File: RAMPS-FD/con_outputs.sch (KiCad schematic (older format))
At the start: 28 parts, among them P218 EXT3, P403 D9_EXT, P404 D8_HB, P405 D10_EXT1, Q201 IRLB8743PBF, Q202 IRLB8743PBF, Q203 IRLB8743PBF, Q204 2N7002, Q205 2N7002, Q206 IRLB8743PBF, Q501 2N7002, Q502 2N7002

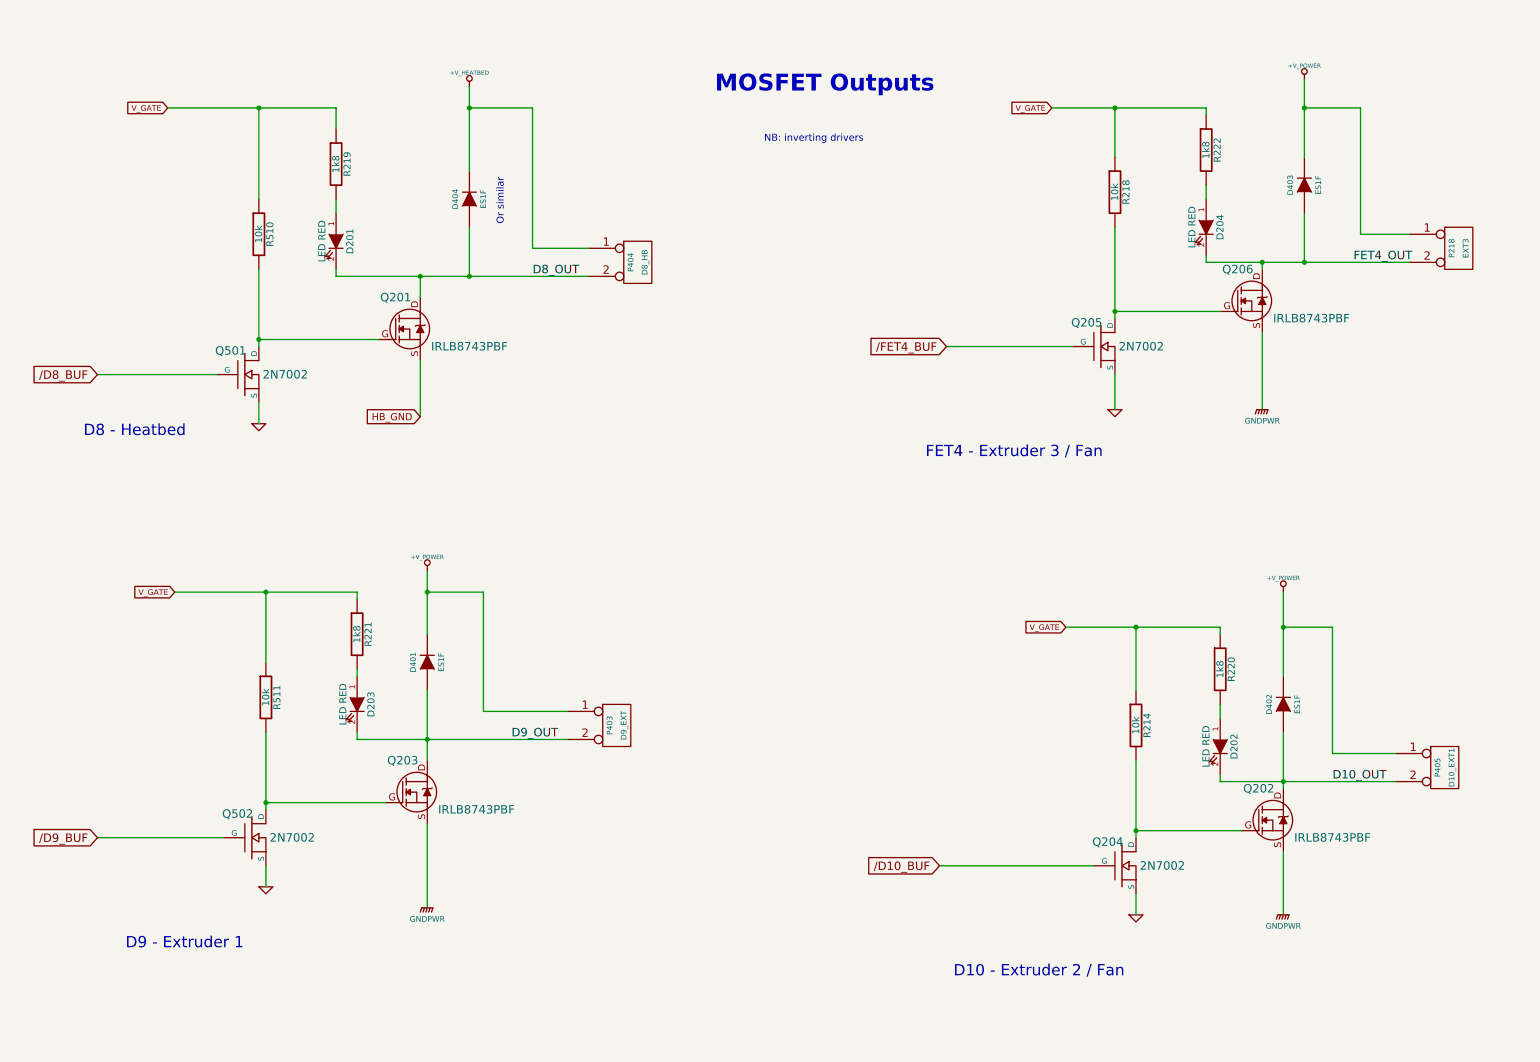
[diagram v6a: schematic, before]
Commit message: RAMPS-FD: update schematic, layout
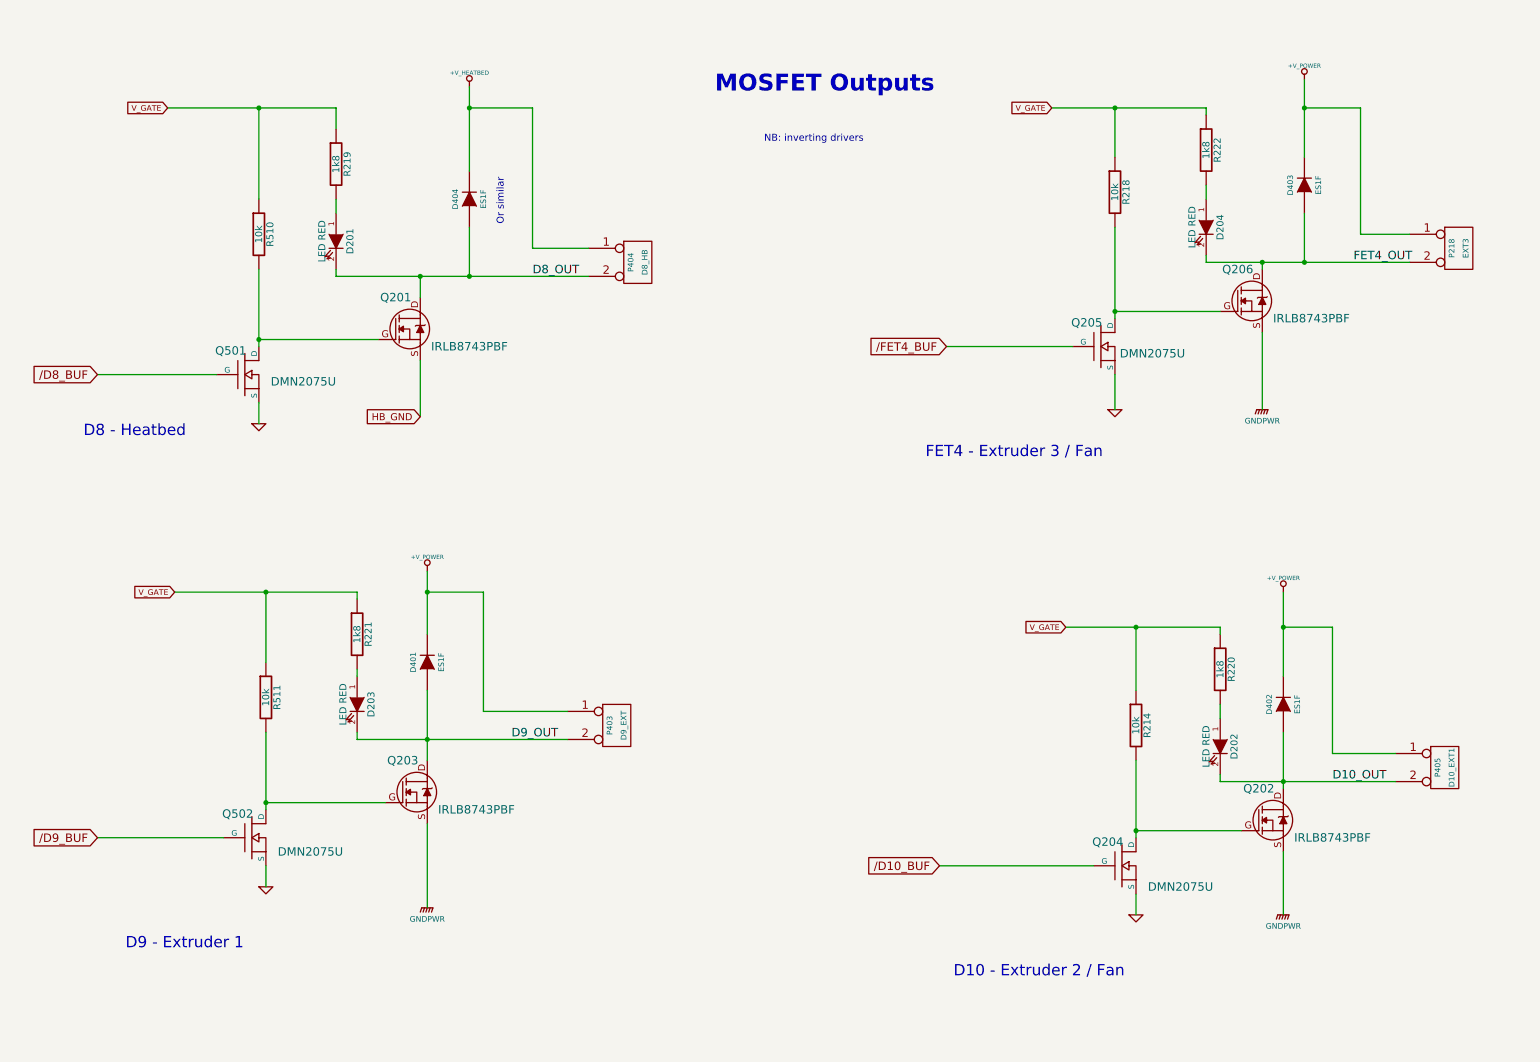
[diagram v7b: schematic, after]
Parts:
- Q204, Q205, Q501, Q502: value 2N7002 -> DMN2075U
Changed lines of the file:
@@
 Sheet 7 9
 Title ""
-Date "24 sep 2013"
+Date "26 sep 2013"
 Rev "0.2"
 Comp ""
@@
 P 2050 2750
 F 0 "Q501" H 2060 2920 60  0000 R CNN
-F 1 "2N7002" H 2500 2750 60  0000 R CNN
+F 1 "DMN2075U" H 2700 2700 60  0000 R CNN
 F 2 "" H 2050 2750 60  0001 C CNN
 F 3 "" H 2050 2750 60  0001 C CNN
@@
 P 2100 6050
 F 0 "Q502" H 2110 6220 60  0000 R CNN
-F 1 "2N7002" H 2550 6050 60  0000 R CNN
+F 1 "DMN2075U" H 2750 5950 60  0000 R CNN
 F 2 "" H 2100 6050 60  0001 C CNN
 F 3 "" H 2100 6050 60  0001 C CNN
@@
 P 8150 2550
 F 0 "Q205" H 8160 2720 60  0000 R CNN
-F 1 "2N7002" H 8600 2550 60  0000 R CNN
+F 1 "DMN2075U" H 8750 2500 60  0000 R CNN
 F 2 "" H 8150 2550 60  0001 C CNN
 F 3 "" H 8150 2550 60  0001 C CNN
@@
 P 8300 6250
 F 0 "Q204" H 8310 6420 60  0000 R CNN
-F 1 "2N7002" H 8750 6250 60  0000 R CNN
+F 1 "DMN2075U" H 8950 6100 60  0000 R CNN
 F 2 "" H 8300 6250 60  0001 C CNN
 F 3 "" H 8300 6250 60  0001 C CNN

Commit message: RAMPS-FD: version 1 Rev A
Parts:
- P218: value EXT3 -> D11
- P403: value D9_EXT -> D9
- P404: value D8_HB -> D8
- P405: value D10_EXT1 -> D10
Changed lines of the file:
@@
 Sheet 7 9
 Title ""
-Date "26 sep 2013"
+Date "3 oct 2013"
 Rev "0.2"
 Comp ""
@@
 V_GATE
 $Comp
-L GND #PWR088
+L GND #PWR089
 U 1 1 51B37840
 P 2150 3100
-F 0 "#PWR088" H 2150 3100 30  0001 C CNN
+F 0 "#PWR089" H 2150 3100 30  0001 C CNN
 F 1 "GND" H 2150 3030 30  0001 C CNN
 F 2 "" H 2150 3100 60  0001 C CNN
@@
 $EndComp
 $Comp
-L GND #PWR089
+L GND #PWR090
 U 1 1 51B377DD
 P 2200 6400
-F 0 "#PWR089" H 2200 6400 30  0001 C CNN
+F 0 "#PWR090" H 2200 6400 30  0001 C CNN
 F 1 "GND" H 2200 6330 30  0001 C CNN
 F 2 "" H 2200 6400 60  0001 C CNN
@@
 D8 - Heatbed
 $Comp
-L GNDPWR #PWR090
+L GNDPWR #PWR091
 U 1 1 51AA07E6
 P 9300 3000
-F 0 "#PWR090" H 9300 3050 40  0001 C CNN
+F 0 "#PWR091" H 9300 3050 40  0001 C CNN
 F 1 "GNDPWR" H 9300 2920 40  0000 C CNN
 F 2 "" H 9300 3000 60  0001 C CNN
@@
 $EndComp
 $Comp
-L GND #PWR091
+L GND #PWR092
 U 1 1 51AA071A
 P 8400 6600
-F 0 "#PWR091" H 8400 6600 30  0001 C CNN
+F 0 "#PWR092" H 8400 6600 30  0001 C CNN
 F 1 "GND" H 8400 6530 30  0001 C CNN
 F 2 "" H 8400 6600 60  0001 C CNN
@@
 $EndComp
 $Comp
-L GNDPWR #PWR092
+L GNDPWR #PWR093
 U 1 1 51AA0719
 P 9450 6600
-F 0 "#PWR092" H 9450 6650 40  0001 C CNN
+F 0 "#PWR093" H 9450 6650 40  0001 C CNN
 F 1 "GNDPWR" H 9450 6520 40  0000 C CNN
 F 2 "" H 9450 6600 60  0001 C CNN
@@
 HB_GND
 $Comp
-L GNDPWR #PWR093
+L GNDPWR #PWR094
 U 1 1 51AA06B9
 P 3350 6550
-F 0 "#PWR093" H 3350 6600 40  0001 C CNN
+F 0 "#PWR094" H 3350 6600 40  0001 C CNN
 F 1 "GNDPWR" H 3350 6470 40  0000 C CNN
 F 2 "" H 3350 6550 60  0001 C CNN
@@
 P 10600 5550
 F 0 "P405" V 10550 5550 40  0000 C CNN
-F 1 "D10_EXT1" V 10650 5550 40  0000 C CNN
+F 1 "D10" V 10650 5550 40  0000 C CNN
 F 2 "" H 10600 5550 60  0001 C CNN
 F 3 "" H 10600 5550 60  0001 C CNN
@@
 P 4700 5250
 F 0 "P403" V 4650 5250 40  0000 C CNN
-F 1 "D9_EXT" V 4750 5250 40  0000 C CNN
+F 1 "D9" V 4750 5250 40  0000 C CNN
 F 2 "" H 4700 5250 60  0001 C CNN
 F 3 "" H 4700 5250 60  0001 C CNN
@@
 P 4850 1950
 F 0 "P404" V 4800 1950 40  0000 C CNN
-F 1 "D8_HB" V 4900 1950 40  0000 C CNN
+F 1 "D8" V 4900 1950 40  0000 C CNN
 F 2 "" H 4850 1950 60  0001 C CNN
 F 3 "" H 4850 1950 60  0001 C CNN
@@
 P 10700 1850
 F 0 "P218" V 10650 1850 40  0000 C CNN
-F 1 "EXT3" V 10750 1850 40  0000 C CNN
+F 1 "D11" V 10750 1850 40  0000 C CNN
 F 2 "" H 10700 1850 60  0001 C CNN
 F 3 "" H 10700 1850 60  0001 C CNN
@@
 $EndComp
 $Comp
-L GND #PWR094
+L GND #PWR095
 U 1 1 51770EF7
 P 8250 3000
-F 0 "#PWR094" H 8250 3000 30  0001 C CNN
+F 0 "#PWR095" H 8250 3000 30  0001 C CNN
 F 1 "GND" H 8250 2930 30  0001 C CNN
 F 2 "" H 8250 3000 60  0001 C CNN
@@
 $EndComp
 $Comp
-L +V_POWER #PWR095
+L +V_POWER #PWR096
 U 1 1 51770EF2
 P 9600 650
-F 0 "#PWR095" H 9600 620 30  0001 C CNN
+F 0 "#PWR096" H 9600 620 30  0001 C CNN
 F 1 "+V_POWER" H 9600 750 30  0000 C CNN
 F 2 "" H 9600 650 60  0001 C CNN
@@
 D8_OUT
 $Comp
-L +V_POWER #PWR096
+L +V_POWER #PWR097
 U 1 1 5176EF23
 P 3350 4150
-F 0 "#PWR096" H 3350 4120 30  0001 C CNN
+F 0 "#PWR097" H 3350 4120 30  0001 C CNN
 F 1 "+V_POWER" H 3350 4250 30  0000 C CNN
 F 2 "" H 3350 4150 60  0001 C CNN
@@
 $EndComp
 $Comp
-L +V_POWER #PWR097
+L +V_POWER #PWR098
 U 1 1 5176EE9D
 P 9450 4300
-F 0 "#PWR097" H 9450 4270 30  0001 C CNN
+F 0 "#PWR098" H 9450 4270 30  0001 C CNN
 F 1 "+V_POWER" H 9450 4400 30  0000 C CNN
 F 2 "" H 9450 4300 60  0001 C CNN
@@
 $EndComp
 $Comp
-L +V_HEATBED #PWR098
+L +V_HEATBED #PWR099
 U 1 1 5176EDD7
 P 3650 700
-F 0 "#PWR098" H 3650 670 30  0001 C CNN
+F 0 "#PWR099" H 3650 670 30  0001 C CNN
 F 1 "+V_HEATBED" H 3650 800 30  0000 C CNN
 F 2 "" H 3650 700 60  0001 C CNN
